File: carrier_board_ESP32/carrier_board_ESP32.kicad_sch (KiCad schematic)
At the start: 7 parts, among them J1 BME280, J2 LTR390, J3 ENS160 I2C, J4 ENS160 SPI, J5 ENS160 + AHT21, J6 DC MOTOR, U1 ESP32-S3-DEVKITC-1-N8R2

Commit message: PCB designing
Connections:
- net GENERATOR_OUTPUT: now reaches J6.1 (Pin_1)
- net GND: now reaches J6.2 (Pin_2)
- net GND: now also J1.2 (Pin_2), J2.3 (Pin_3), J3.3 (Pin_3), J4.2 (Pin_2), J5.3 (Pin_3)
- net SDA: now reaches J3.1 (Pin_1)
- net SDA: now also J1.4 (Pin_4), J2.5 (Pin_5), J5.5 (Pin_5)
- net SCL: now reaches J3.2 (Pin_2)
- net SCL: now also J1.3 (Pin_3), J2.4 (Pin_4), J5.4 (Pin_4)
- net 3V3: now reaches J3.4 (Pin_4)
- net 3V3: now also J2.2 (Pin_2), J4.1 (Pin_1), J5.2 (Pin_2)
- net SCK: now reaches J4.3 (Pin_3)
- net SDI: now reaches J4.4 (Pin_4)
- net SDO: now reaches J4.5 (Pin_5)
- net SDO: now also J1.6 (Pin_6)
- net CS: now reaches J4.6 (Pin_6)
- net CS: now also J5.7 (Pin_7)
- net INT: now reaches J4.7 (Pin_7)
- net INT: now also J2.6 (Pin_6), J5.8 (Pin_8)
- net VCC: now reaches J1.1 (Pin_1)
- net CSB: now reaches J1.5 (Pin_5)
- net VIN: now reaches J2.1 (Pin_1)
- net VIN: now also J5.1 (Pin_1)
- net ADD: now reaches J5.6 (Pin_6)

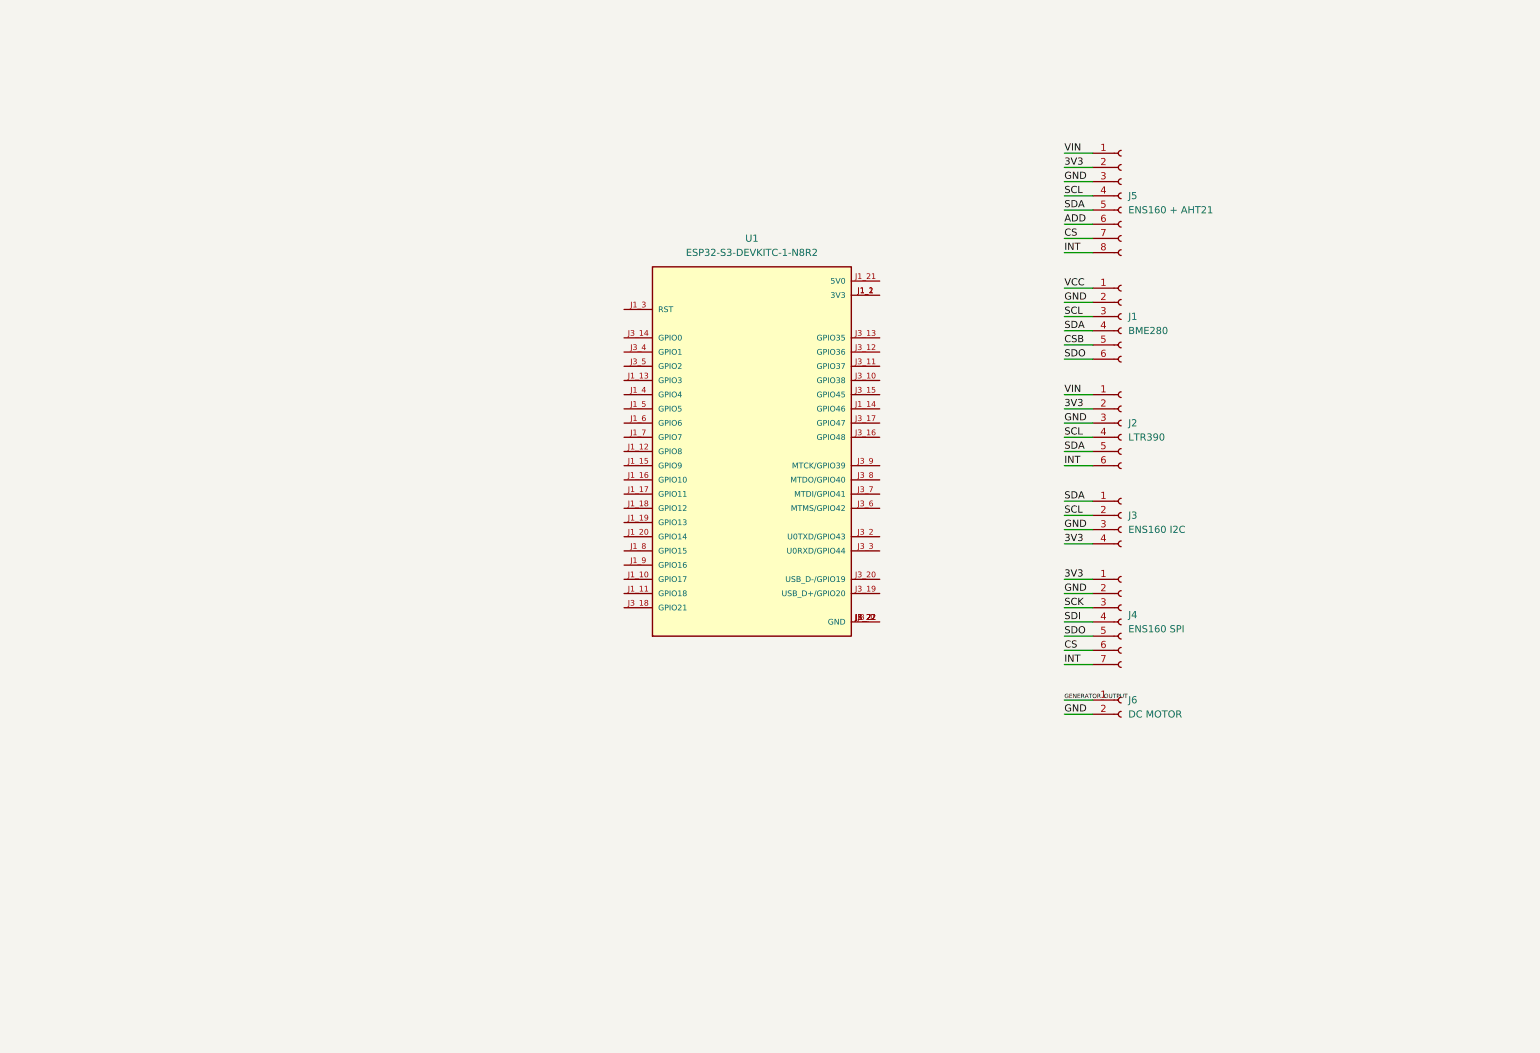
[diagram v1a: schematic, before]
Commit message: added power supply (battery and solar panel)
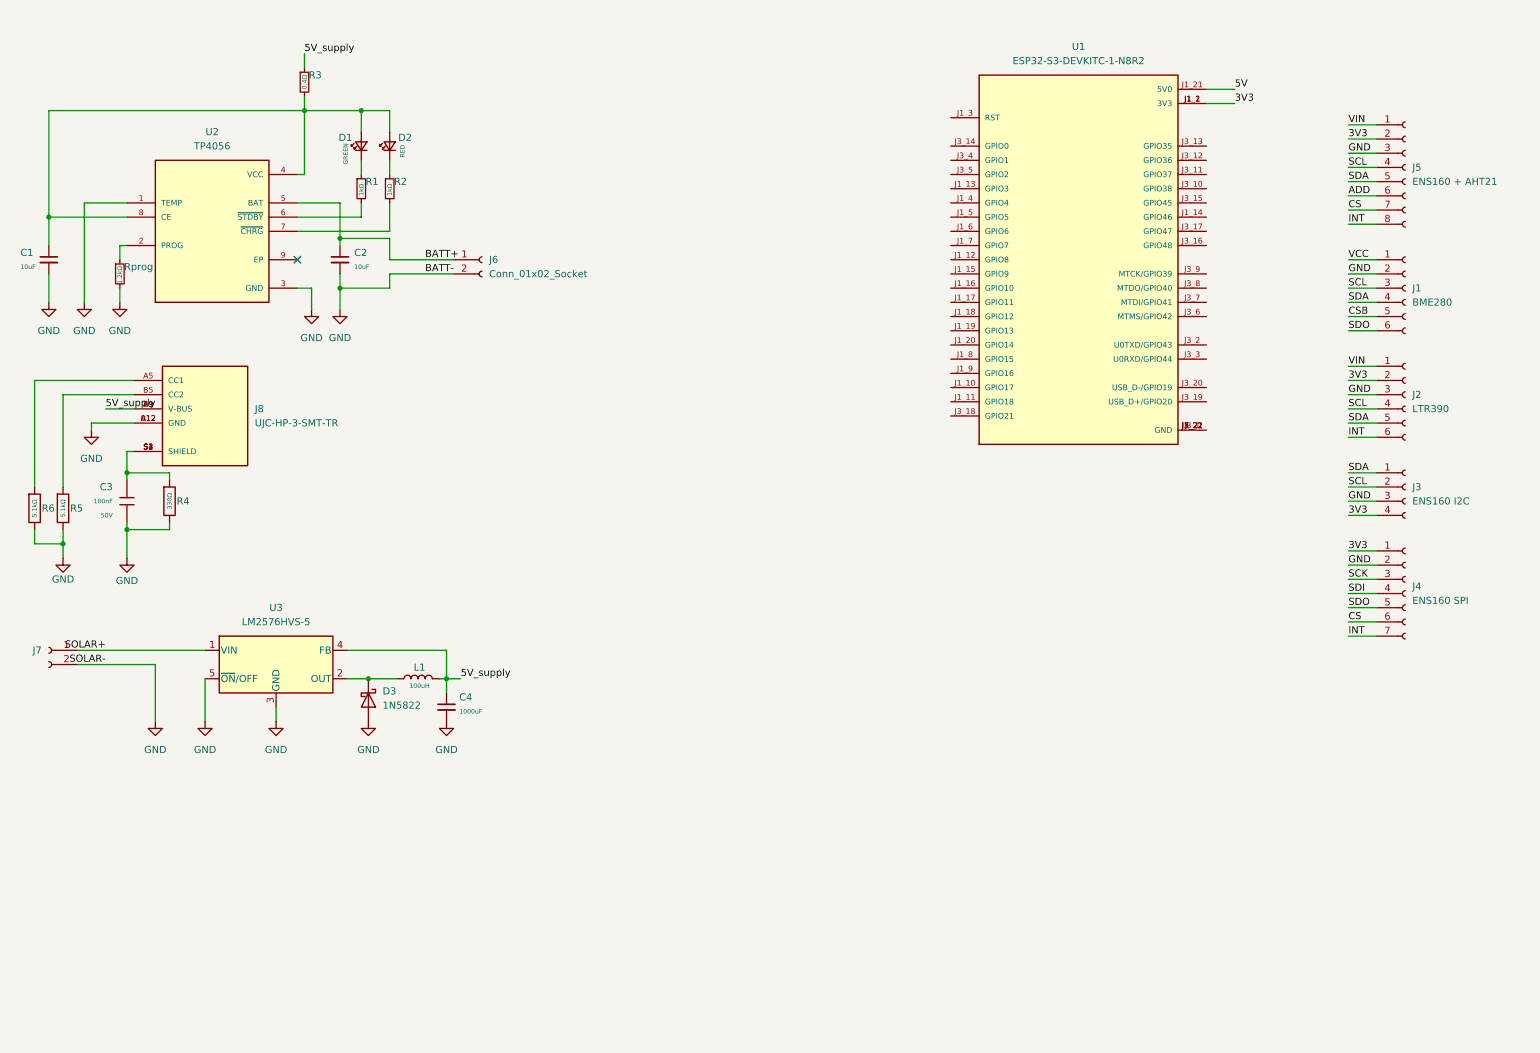
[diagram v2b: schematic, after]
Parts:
- added C1, C2: 10uF, symbol Device:C_Small
- added C3: 100nF, PCM_JLCPCB:C_0402, symbol PCM_JLCPCB-Capacitors:0402,100nF,(2)
- added C4: 1000uF, symbol Device:C_Small
- added D1: GREEN, symbol Device:LED_Small
- added D2: RED, symbol Device:LED_Small
- added D3: 1N5822, Diode_THT:D_DO-201AD_P15.24mm_Horizontal, symbol Diode:1N5822
- added J7: Conn_01x02_Socket, Connector_AMASS:AMASS_XT30UPB-F_1x02_P5.0mm_Vertical, symbol Connector:Conn_01x02_Socket
- added J8: UJC-HP-3-SMT-TR, UJC-HP-3-SMT-TR:CUI_UJC-HP-3-SMT-TR, symbol UJC-HP-3-SMT-TR:UJC-HP-3-SMT-TR
- added L1: 100uH, symbol Device:L
- added R1, R2: 1kΩ, symbol Device:R_Small
- added R3: 0.4Ω, symbol Device:R_Small
- added R4: 330Ω, PCM_JLCPCB:R_0402, symbol PCM_JLCPCB-Resistors:0402,330Ω
- added R5, R6: 5.1kΩ, PCM_JLCPCB:R_0402, symbol PCM_JLCPCB-Resistors:0402,5.1kΩ
- added Rprog: 1.2kΩ, symbol Device:R_Small
- added U2: TP4056, TP4056:SOP127P600X175-9N, symbol TP4056:TP4056
- added U3: LM2576HVS-5, Package_TO_SOT_SMD:TO-263-5_TabPin3, symbol Regulator_Switching:LM2576HVS-5
- J1, J2: footprint (none) -> Connector_PinHeader_1.00mm:PinHeader_1x06_P1.00mm_Vertical
- J3: footprint (none) -> Connector_PinHeader_1.00mm:PinHeader_1x04_P1.00mm_Vertical
- J4: footprint (none) -> Connector_PinHeader_1.00mm:PinHeader_1x07_P1.00mm_Vertical
- J5: footprint (none) -> Connector_PinHeader_1.00mm:PinHeader_1x08_P1.00mm_Vertical
- J6: value DC MOTOR -> Conn_01x02_Socket; footprint (none) -> Connector_AMASS:AMASS_XT30UPB-F_1x02_P5.0mm_Vertical
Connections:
- net 3V3: now also U1.J1_1 (3V3), U1.J1_2 (3V3)
- net GND: now also C1.2, C2.2, C3.2, C4.2, D3.2 (A), J7.2 (Pin_2), J8.A12 (GND), J8.B12 (GND), R4.2, R5.2, R6.2, Rprog.2, U2.1 (TEMP), U2.3 (GND), U3.3 (GND), U3.5 (~{ON}/OFF)
- net 5V: now reaches U1.J1_21 (5V0)
- net GENERATOR_OUTPUT renamed BATT+
- net BATT+: now also C2.1, U2.5 (BAT)
- new net: D2.1 (K), R2.1
- new net: C1.1, D1.2 (A), D2.2 (A), R3.2, U2.4 (VCC), U2.8 (CE)
- new net: D1.1 (K), R1.1
- new net: R1.2, U2.6 (~{STDBY})
- new net: J8.A5 (CC1), R6.1
- new net: J8.B5 (CC2), R5.1
- new net: C3.1, J8.S1 (SHIELD), J8.S2 (SHIELD), J8.S3 (SHIELD), J8.S4 (SHIELD), R4.1
- new net: D3.1 (K), L1.1, U3.2 (OUT)
- new net: Rprog.1, U2.2 (PROG)
- new net: R2.2, U2.7 (~{CHRG})
- new net 5V_supply: C4.1, J8.A9 (V-BUS), J8.B9 (V-BUS), L1.2, R3.1, U3.4 (FB)
- new net SOLAR+: J7.1 (Pin_1), U3.1 (VIN)
- no-connect marks 0 -> 1
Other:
- moved on the sheet: J1, J2, J3, J4, J5, U1

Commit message: completed supply section
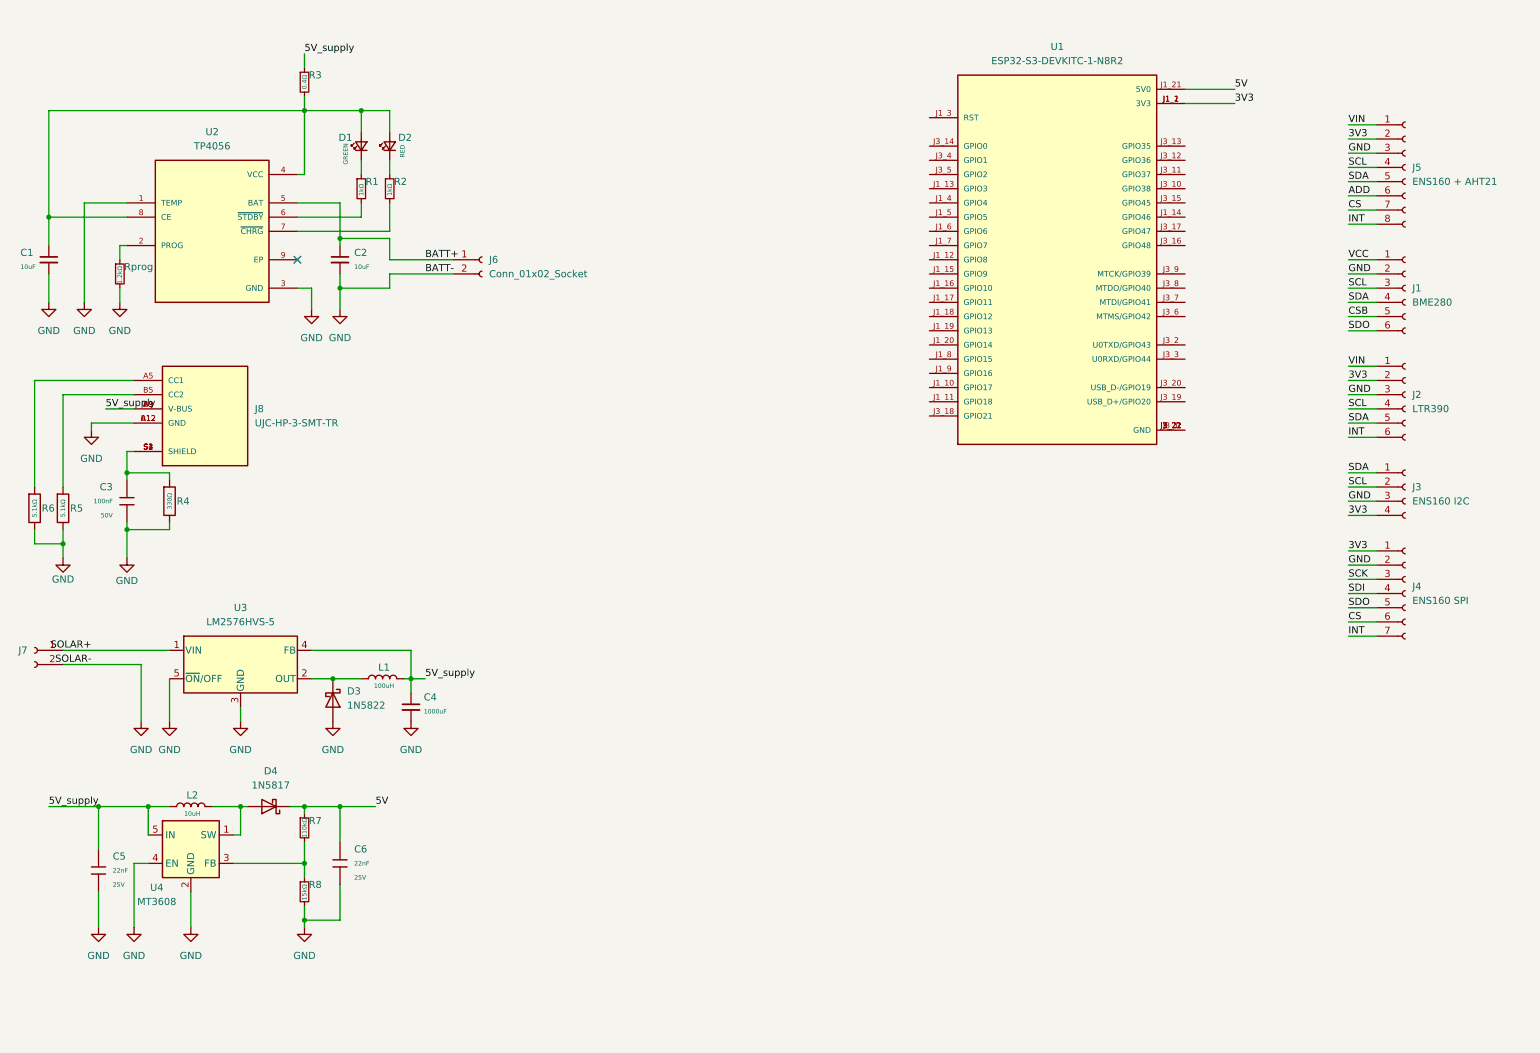
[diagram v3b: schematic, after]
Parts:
- added C5, C6: 22nF, PCM_JLCPCB:C_0402, symbol PCM_JLCPCB-Capacitors:0402,100nF,(2)
- added D4: 1N5817, Diode_THT:D_DO-41_SOD81_P10.16mm_Horizontal, symbol Diode:1N5817
- added L2: 10uH, symbol Device:L
- added R7: 110kΩ, symbol Device:R_Small
- added R8: 15kΩ, symbol Device:R_Small
- added U4: MT3608, Package_TO_SOT_SMD:SOT-23-6, symbol Regulator_Switching:MT3608
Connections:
- net 5V: now also C6.1, D4.1 (K), R7.1
- net 5V_supply: now also C5.1, L2.1, U4.5 (IN)
- net GND: now also C5.2, C6.2, R8.2, U4.2 (GND), U4.4 (EN)
- new net: D4.2 (A), L2.2, U4.1 (SW)
- new net: R7.2, R8.1, U4.3 (FB)
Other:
- moved on the sheet: C4, D3, J7, L1, U1, U3

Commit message: added hall sensor for wind speed and direction mesuring
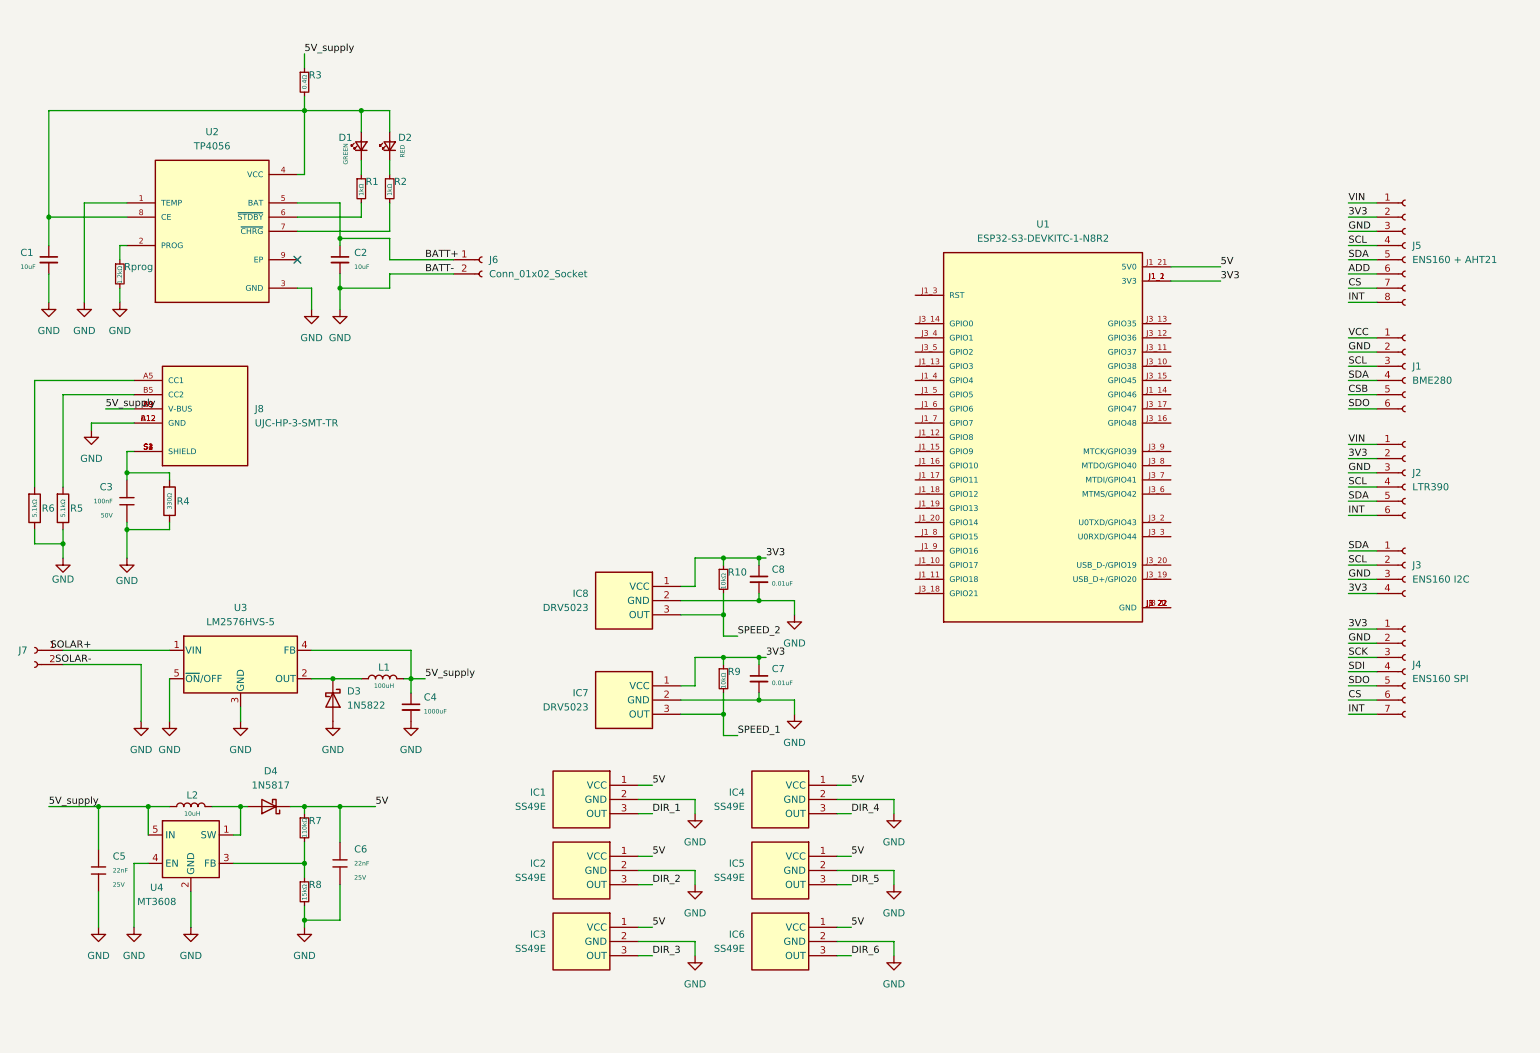
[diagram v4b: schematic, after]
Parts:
- added C7, C8: 0.01uF, symbol Device:C_Small
- added IC1, IC2, IC3, IC4, IC5, IC6: SS49E, TO130P160X410X300-3P, symbol SS49E:SS49E
- added IC7, IC8: DRV5023, TO130P160X410X300-3P, symbol SS49E:SS49E
- added R10, R9: 10kΩ, symbol Device:R_Small
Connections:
- net 3V3: now also C7.1, C8.1, IC7.1 (VCC), IC8.1 (VCC), R10.1, R9.1
- net 5V: now also IC1.1 (VCC), IC2.1 (VCC), IC3.1 (VCC), IC4.1 (VCC), IC5.1 (VCC), IC6.1 (VCC)
- net GND: now also C7.2, C8.2, IC1.2 (GND), IC2.2 (GND), IC3.2 (GND), IC4.2 (GND), IC5.2 (GND), IC6.2 (GND), IC7.2 (GND), IC8.2 (GND)
- new net DIR_1: IC1.3 (OUT)
- new net DIR_2: IC2.3 (OUT)
- new net DIR_3: IC3.3 (OUT)
- new net DIR_4: IC4.3 (OUT)
- new net DIR_5: IC5.3 (OUT)
- new net DIR_6: IC6.3 (OUT)
- new net SPEED_1: IC7.3 (OUT), R9.2
- new net SPEED_2: IC8.3 (OUT), R10.2
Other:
- moved on the sheet: J1, J2, J3, J4, J5, U1
